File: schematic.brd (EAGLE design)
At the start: 108.2 x 139.7 mm, 126 parts, among them IC1 AD8015, IC2 AD8015, IC3 AD8015, IC4 AD8015

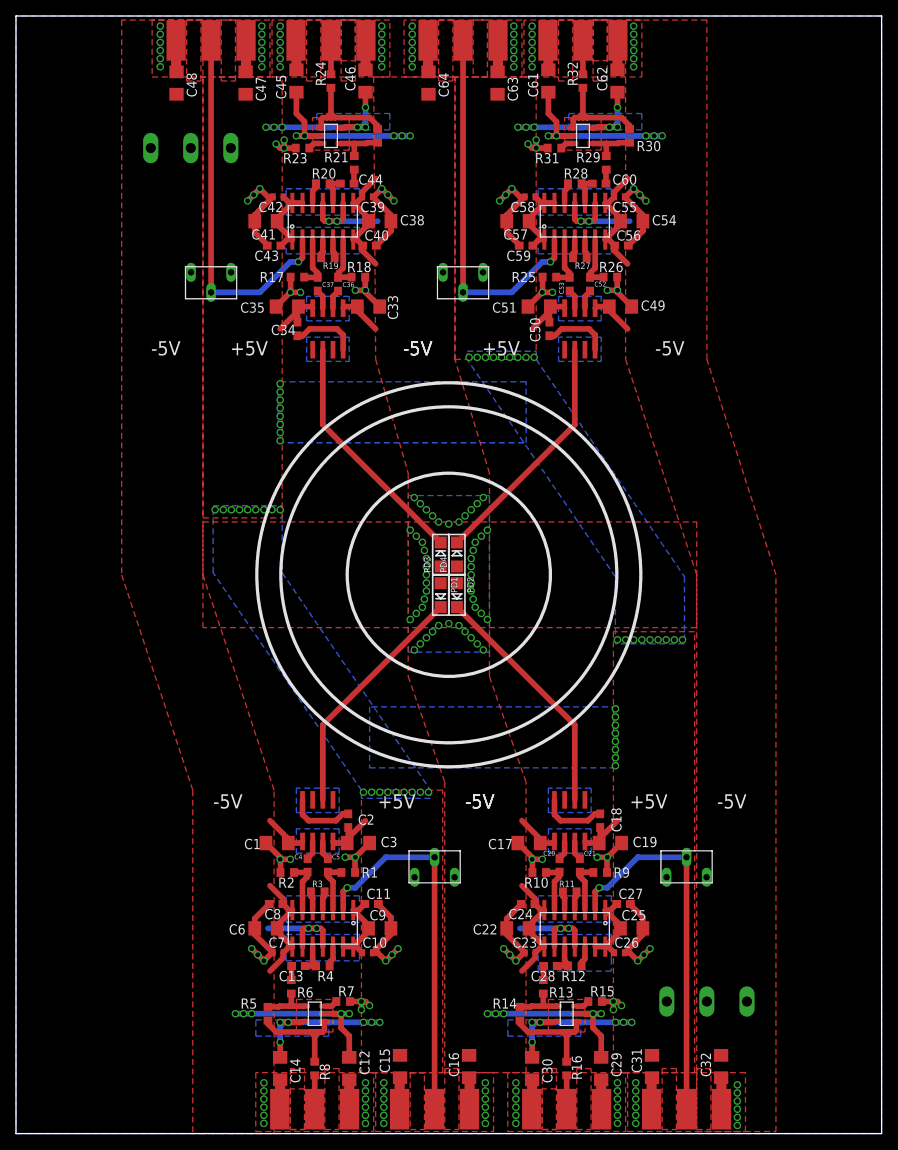
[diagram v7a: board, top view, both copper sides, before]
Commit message: Fixed unrouted, added top gnd plane
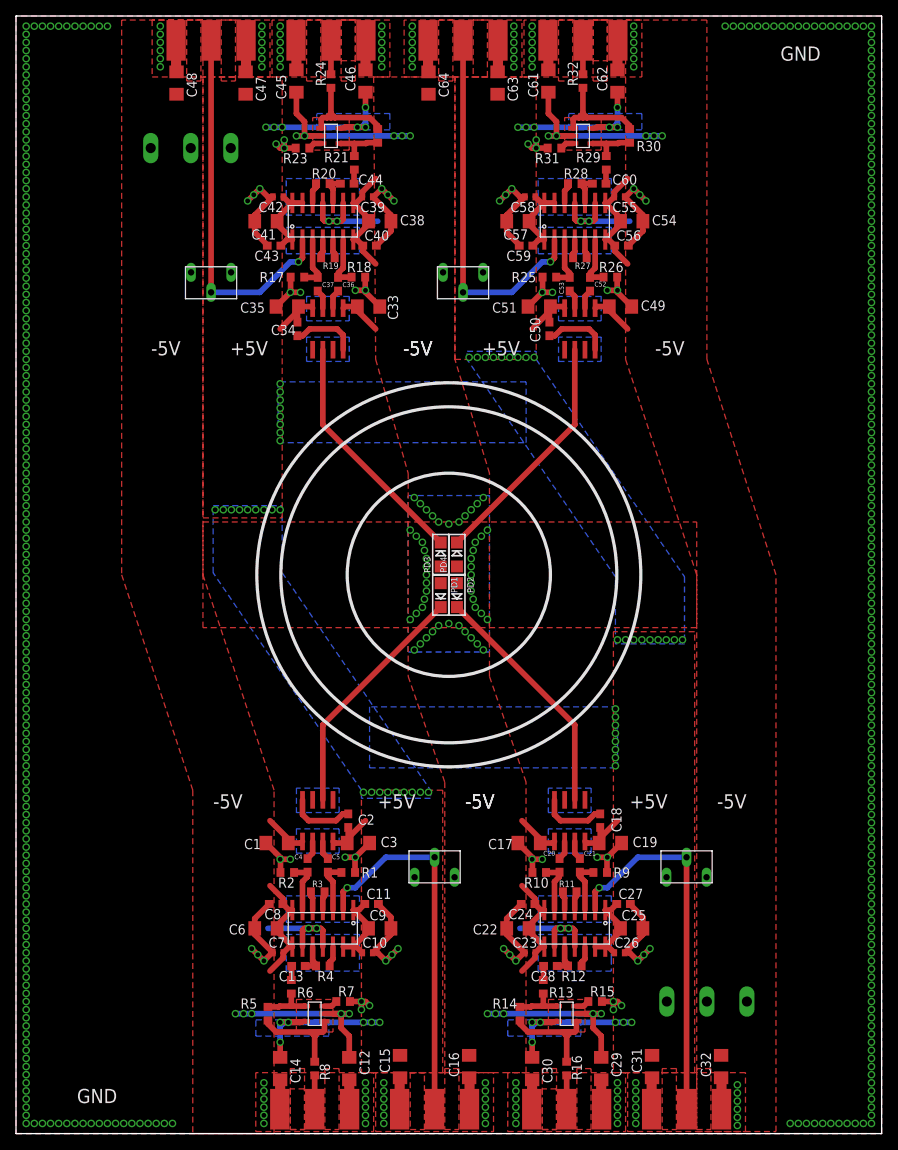
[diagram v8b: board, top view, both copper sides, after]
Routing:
- net GND: vias 156 -> 484
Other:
- board text added: "GND"
